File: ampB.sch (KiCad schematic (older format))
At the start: 13 parts, among them U4 screw_term, U5 Mux, U6 MCP6004, U7 screw_term

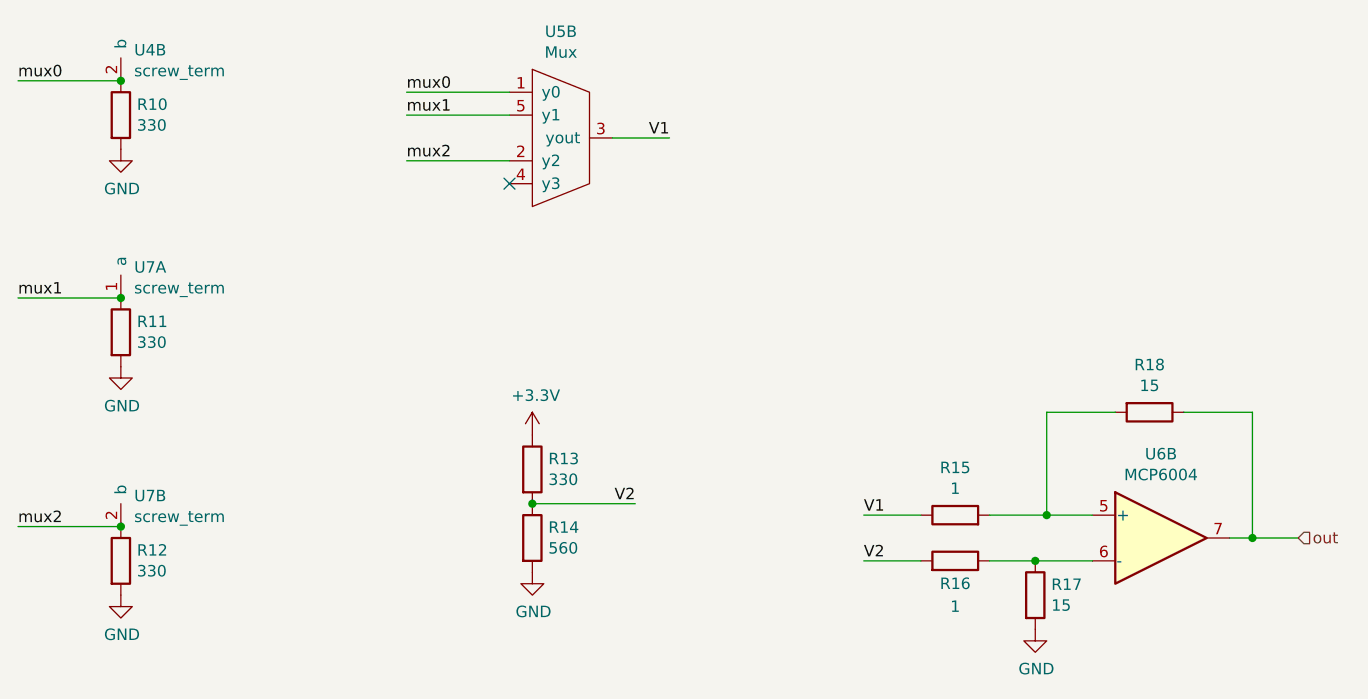
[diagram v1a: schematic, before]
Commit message: switched to sensor sheet for one sensor divider
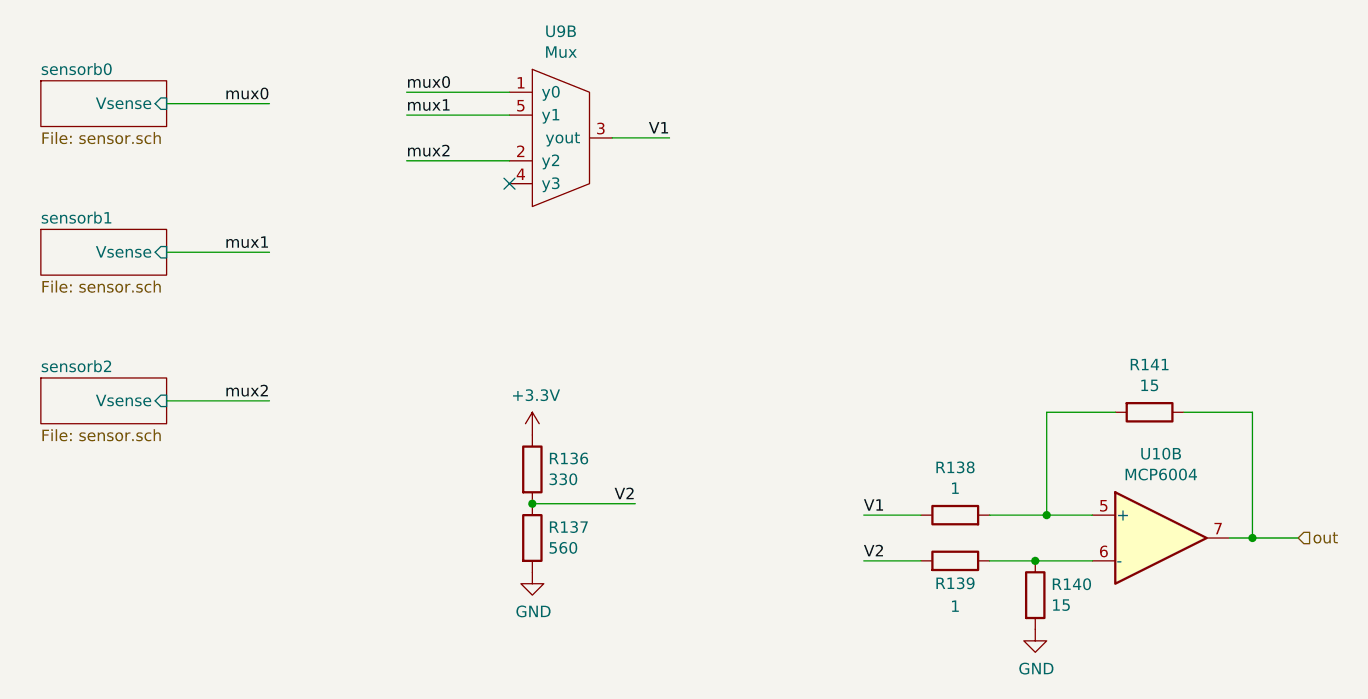
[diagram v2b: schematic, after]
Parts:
- removed R10, R11, R12: 330, Resistor_THT:R_Axial_DIN0204_L3.6mm_D1.6mm_P5.08mm_Horizontal, symbol Device:R
- removed U4, U7: screw_term, Connector_PinHeader_1.27mm:PinHeader_1x02_P1.27mm_Vertical, symbol PNG_PCB_Parts:screw_term
- renumbered R13 to R16, R14 to R17, R15 to R18, R16 to R19, R17 to R20, R18 to R21, U5 to U3, U6 to U4

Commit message: revised sensor connector
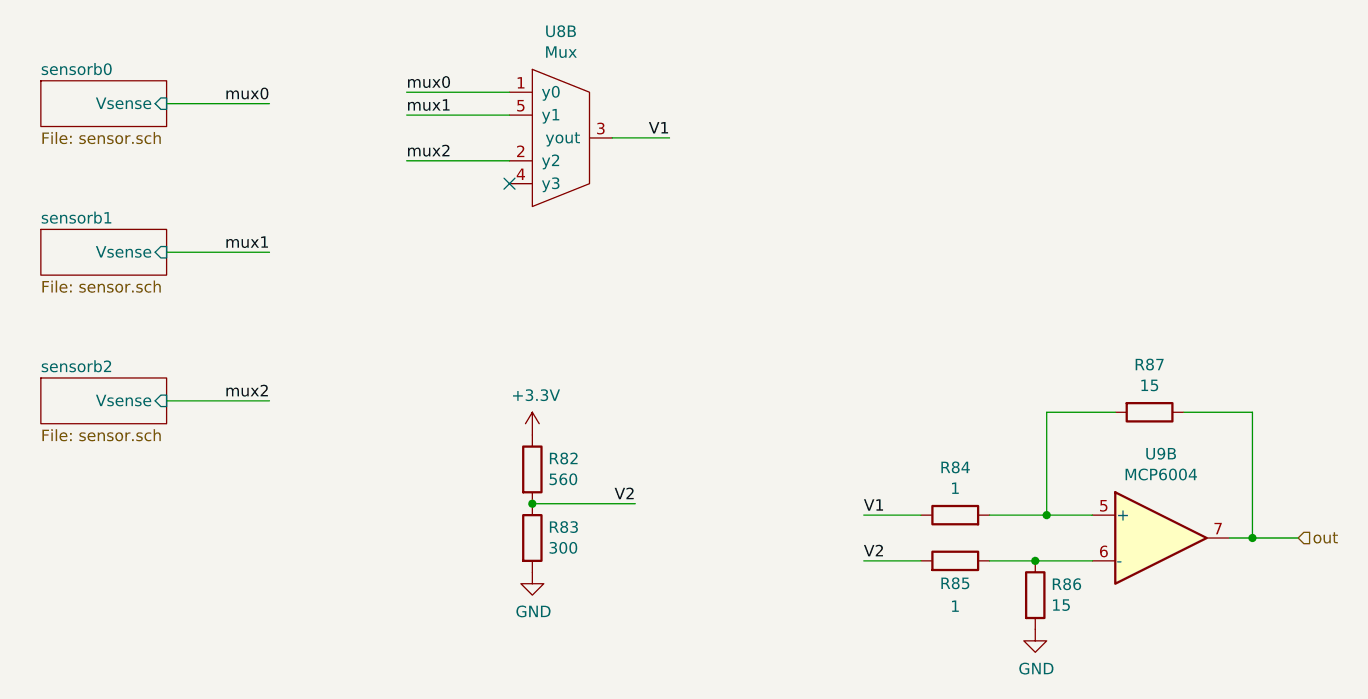
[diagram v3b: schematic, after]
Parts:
- R10: renamed from R16; value 330 -> 560
- R11: renamed from R17; value 560 -> 300
- renumbered R18 to R12, R19 to R13, R20 to R14, R21 to R15, U3 to U2, U4 to U3
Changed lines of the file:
@@
 $Descr A4 11693 8268
 encoding utf-8
-Sheet 6 41
+Sheet 38 41
 Title ""
 Date ""
@@
 AR Path="/6017CC5E/6019E3A5" Ref="R?"  Part="1"
 AR Path="/6017DA21/6019E3A5" Ref="R?"  Part="1"
-AR Path="/601927EB/6019E3A5" Ref="R20"  Part="1"
+AR Path="/601927EB/6019E3A5" Ref="R14"  Part="1"
 AR Path="/6019DBCE/6019E3A5" Ref="R?"  Part="1"
-AR Path="/601B4C11/6019E3A5" Ref="R80"  Part="1"
-AR Path="/601B73BA/6019E3A5" Ref="R140"  Part="1"
-F 0 "R140" H 5520 4096 50  0000 L CNN
+AR Path="/601B4C11/6019E3A5" Ref="R50"  Part="1"
+AR Path="/601B73BA/6019E3A5" Ref="R86"  Part="1"
+F 0 "R86" H 5520 4096 50  0000 L CNN
 F 1 "15" H 5520 4005 50  0000 L CNN
 F 2 "Resistor_THT:R_Axial_DIN0204_L3.6mm_D1.6mm_P5.08mm_Horizontal" V 5380 4050 50  0001 C CNN
@@
 AR Path="/6017CC5E/6017E430" Ref="R?"  Part="1"
 AR Path="/6017DA21/6017E430" Ref="R?"  Part="1"
-AR Path="/601927EB/6017E430" Ref="R21"  Part="1"
+AR Path="/601927EB/6017E430" Ref="R15"  Part="1"
 AR Path="/6019DBCE/6017E430" Ref="R?"  Part="1"
-AR Path="/601B4C11/6017E430" Ref="R81"  Part="1"
-AR Path="/601B73BA/6017E430" Ref="R141"  Part="1"
-F 0 "R141" V 5743 3250 50  0000 C CNN
+AR Path="/601B4C11/6017E430" Ref="R51"  Part="1"
+AR Path="/601B73BA/6017E430" Ref="R87"  Part="1"
+F 0 "R87" V 5743 3250 50  0000 C CNN
 F 1 "15" V 5834 3250 50  0000 C CNN
 F 2 "Resistor_THT:R_Axial_DIN0204_L3.6mm_D1.6mm_P5.08mm_Horizontal" V 5880 3250 50  0001 C CNN
@@
 AR Path="/6017CC5E/60198F33" Ref="R?"  Part="1"
 AR Path="/6017DA21/60198F33" Ref="R?"  Part="1"
-AR Path="/601927EB/60198F33" Ref="R18"  Part="1"
+AR Path="/601927EB/60198F33" Ref="R12"  Part="1"
 AR Path="/6019DBCE/60198F33" Ref="R?"  Part="1"
-AR Path="/601B4C11/60198F33" Ref="R78"  Part="1"
-AR Path="/601B73BA/60198F33" Ref="R138"  Part="1"
-F 0 "R138" V 5307 3700 50  0000 C CNN
+AR Path="/601B4C11/60198F33" Ref="R48"  Part="1"
+AR Path="/601B73BA/60198F33" Ref="R84"  Part="1"
+F 0 "R84" V 5307 3700 50  0000 C CNN
 F 1 "1" V 5216 3700 50  0000 C CNN
 F 2 "Resistor_THT:R_Axial_DIN0204_L3.6mm_D1.6mm_P5.08mm_Horizontal" V 5030 3700 50  0001 C CNN
@@
 AR Path="/6017CC5E/6017E432" Ref="R?"  Part="1"
 AR Path="/6017DA21/6017E432" Ref="R?"  Part="1"
-AR Path="/601927EB/6017E432" Ref="R19"  Part="1"
+AR Path="/601927EB/6017E432" Ref="R13"  Part="1"
 AR Path="/6019DBCE/6017E432" Ref="R?"  Part="1"
-AR Path="/601B4C11/6017E432" Ref="R79"  Part="1"
-AR Path="/601B73BA/6017E432" Ref="R139"  Part="1"
-F 0 "R139" V 5000 3900 50  0000 C CNN
+AR Path="/601B4C11/6017E432" Ref="R49"  Part="1"
+AR Path="/601B73BA/6017E432" Ref="R85"  Part="1"
+F 0 "R85" V 5000 3900 50  0000 C CNN
 F 1 "1" V 4900 3900 50  0000 C CNN
 F 2 "Resistor_THT:R_Axial_DIN0204_L3.6mm_D1.6mm_P5.08mm_Horizontal" V 5030 3900 50  0001 C CNN
@@
 AR Path="/6017CC5E/60198F35" Ref="R?"  Part="1"
 AR Path="/6017DA21/60198F35" Ref="R?"  Part="1"
-AR Path="/601927EB/60198F35" Ref="R16"  Part="1"
+AR Path="/601927EB/60198F35" Ref="R10"  Part="1"
 AR Path="/6019DBCE/60198F35" Ref="R?"  Part="1"
-AR Path="/601B4C11/60198F35" Ref="R76"  Part="1"
-AR Path="/601B73BA/60198F35" Ref="R136"  Part="1"
-F 0 "R136" H 3320 3546 50  0000 L CNN
-F 1 "330" H 3320 3455 50  0000 L CNN
+AR Path="/601B4C11/60198F35" Ref="R46"  Part="1"
+AR Path="/601B73BA/60198F35" Ref="R82"  Part="1"
+F 0 "R82" H 3320 3546 50  0000 L CNN
+F 1 "560" H 3320 3455 50  0000 L CNN
 F 2 "Resistor_THT:R_Axial_DIN0204_L3.6mm_D1.6mm_P5.08mm_Horizontal" V 3180 3500 50  0001 C CNN
 F 3 "~" H 3250 3500 50  0001 C CNN
@@
 AR Path="/6017CC5E/6019E3B4" Ref="R?"  Part="1"
 AR Path="/6017DA21/6019E3B4" Ref="R?"  Part="1"
-AR Path="/601927EB/6019E3B4" Ref="R17"  Part="1"
+AR Path="/601927EB/6019E3B4" Ref="R11"  Part="1"
 AR Path="/6019DBCE/6019E3B4" Ref="R?"  Part="1"
-AR Path="/601B4C11/6019E3B4" Ref="R77"  Part="1"
-AR Path="/601B73BA/6019E3B4" Ref="R137"  Part="1"
-F 0 "R137" H 3320 3846 50  0000 L CNN
-F 1 "560" H 3320 3755 50  0000 L CNN
+AR Path="/601B4C11/6019E3B4" Ref="R47"  Part="1"
+AR Path="/601B73BA/6019E3B4" Ref="R83"  Part="1"
+F 0 "R83" H 3320 3846 50  0000 L CNN
+F 1 "300" H 3320 3755 50  0000 L CNN
 F 2 "Resistor_THT:R_Axial_DIN0204_L3.6mm_D1.6mm_P5.08mm_Horizontal" V 3180 3800 50  0001 C CNN
 F 3 "~" H 3250 3800 50  0001 C CNN
@@
 AR Path="/6017CC5E/6019E3B5" Ref="#PWR?"  Part="1"
 AR Path="/6017DA21/6019E3B5" Ref="#PWR?"  Part="1"
-AR Path="/601927EB/6019E3B5" Ref="#PWR033"  Part="1"
+AR Path="/601927EB/6019E3B5" Ref="#PWR021"  Part="1"
 AR Path="/6019DBCE/6019E3B5" Ref="#PWR?"  Part="1"
-AR Path="/601B4C11/6019E3B5" Ref="#PWR0123"  Part="1"
-AR Path="/601B73BA/6019E3B5" Ref="#PWR0213"  Part="1"
-F 0 "#PWR0213" H 3250 3200 50  0001 C CNN
+AR Path="/601B4C11/6019E3B5" Ref="#PWR063"  Part="1"
+AR Path="/601B73BA/6019E3B5" Ref="#PWR0105"  Part="1"
+F 0 "#PWR0105" H 3250 3200 50  0001 C CNN
 F 1 "+3.3V" H 3265 3523 50  0000 C CNN
 F 2 "" H 3250 3350 50  0001 C CNN
@@
 AR Path="/6017CC5E/6017E436" Ref="#PWR?"  Part="1"
 AR Path="/6017DA21/6017E436" Ref="#PWR?"  Part="1"
-AR Path="/601927EB/6017E436" Ref="#PWR034"  Part="1"
+AR Path="/601927EB/6017E436" Ref="#PWR022"  Part="1"
 AR Path="/6019DBCE/6017E436" Ref="#PWR?"  Part="1"
-AR Path="/601B4C11/6017E436" Ref="#PWR0124"  Part="1"
-AR Path="/601B73BA/6017E436" Ref="#PWR0214"  Part="1"
-F 0 "#PWR0214" H 3250 3700 50  0001 C CNN
+AR Path="/601B4C11/6017E436" Ref="#PWR064"  Part="1"
+AR Path="/601B73BA/6017E436" Ref="#PWR0106"  Part="1"
+F 0 "#PWR0106" H 3250 3700 50  0001 C CNN
 F 1 "GND" H 3255 3777 50  0000 C CNN
 F 2 "" H 3250 3950 50  0001 C CNN
@@
 AR Path="/6017CC5E/6019E3AC" Ref="#PWR?"  Part="1"
 AR Path="/6017DA21/6019E3AC" Ref="#PWR?"  Part="1"
-AR Path="/601927EB/6019E3AC" Ref="#PWR035"  Part="1"
+AR Path="/601927EB/6019E3AC" Ref="#PWR023"  Part="1"
 AR Path="/6019DBCE/6019E3AC" Ref="#PWR?"  Part="1"
-AR Path="/601B4C11/6019E3AC" Ref="#PWR0125"  Part="1"
-AR Path="/601B73BA/6019E3AC" Ref="#PWR0215"  Part="1"
-F 0 "#PWR0215" H 5450 3950 50  0001 C CNN
+AR Path="/601B4C11/6019E3AC" Ref="#PWR065"  Part="1"
+AR Path="/601B73BA/6019E3AC" Ref="#PWR0107"  Part="1"
+F 0 "#PWR0107" H 5450 3950 50  0001 C CNN
 F 1 "GND" H 5455 4027 50  0000 C CNN
 F 2 "" H 5450 4200 50  0001 C CNN
@@
 mux2
 $Comp
-L PNG_PCB_Parts:Mux U3
+L PNG_PCB_Parts:Mux U2
 U 2 1 6017859B
 P 3350 2050
-AR Path="/601927EB/6017859B" Ref="U3"  Part="2"
-AR Path="/601B4C11/6017859B" Ref="U6"  Part="2"
-AR Path="/601B73BA/6017859B" Ref="U9"  Part="2"
-F 0 "U9" H 3375 2515 50  0000 C CNN
+AR Path="/601927EB/6017859B" Ref="U2"  Part="2"
+AR Path="/601B4C11/6017859B" Ref="U5"  Part="2"
+AR Path="/601B73BA/6017859B" Ref="U8"  Part="2"
+F 0 "U8" H 3375 2515 50  0000 C CNN
 F 1 "Mux" H 3375 2424 50  0000 C CNN
 F 2 "Package_DIP:DIP-16_W7.62mm" H 3350 2050 50  0001 C CNN
@@
 $EndComp
 $Comp
-L Amplifier_Operational:MCP6004 U4
+L Amplifier_Operational:MCP6004 U3
 U 2 1 6018C8DB
 P 6000 3800
-AR Path="/601927EB/6018C8DB" Ref="U4"  Part="2"
-AR Path="/601B4C11/6018C8DB" Ref="U7"  Part="2"
-AR Path="/601B73BA/6018C8DB" Ref="U10"  Part="2"
-F 0 "U10" H 6000 4167 50  0000 C CNN
+AR Path="/601927EB/6018C8DB" Ref="U3"  Part="2"
+AR Path="/601B4C11/6018C8DB" Ref="U6"  Part="2"
+AR Path="/601B73BA/6018C8DB" Ref="U9"  Part="2"
+F 0 "U9" H 6000 4167 50  0000 C CNN
 F 1 "MCP6004" H 6000 4076 50  0000 C CNN
 F 2 "Package_DIP:DIP-14_W7.62mm" H 5950 3900 50  0001 C CNN
